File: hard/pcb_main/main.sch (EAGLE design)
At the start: 155 parts

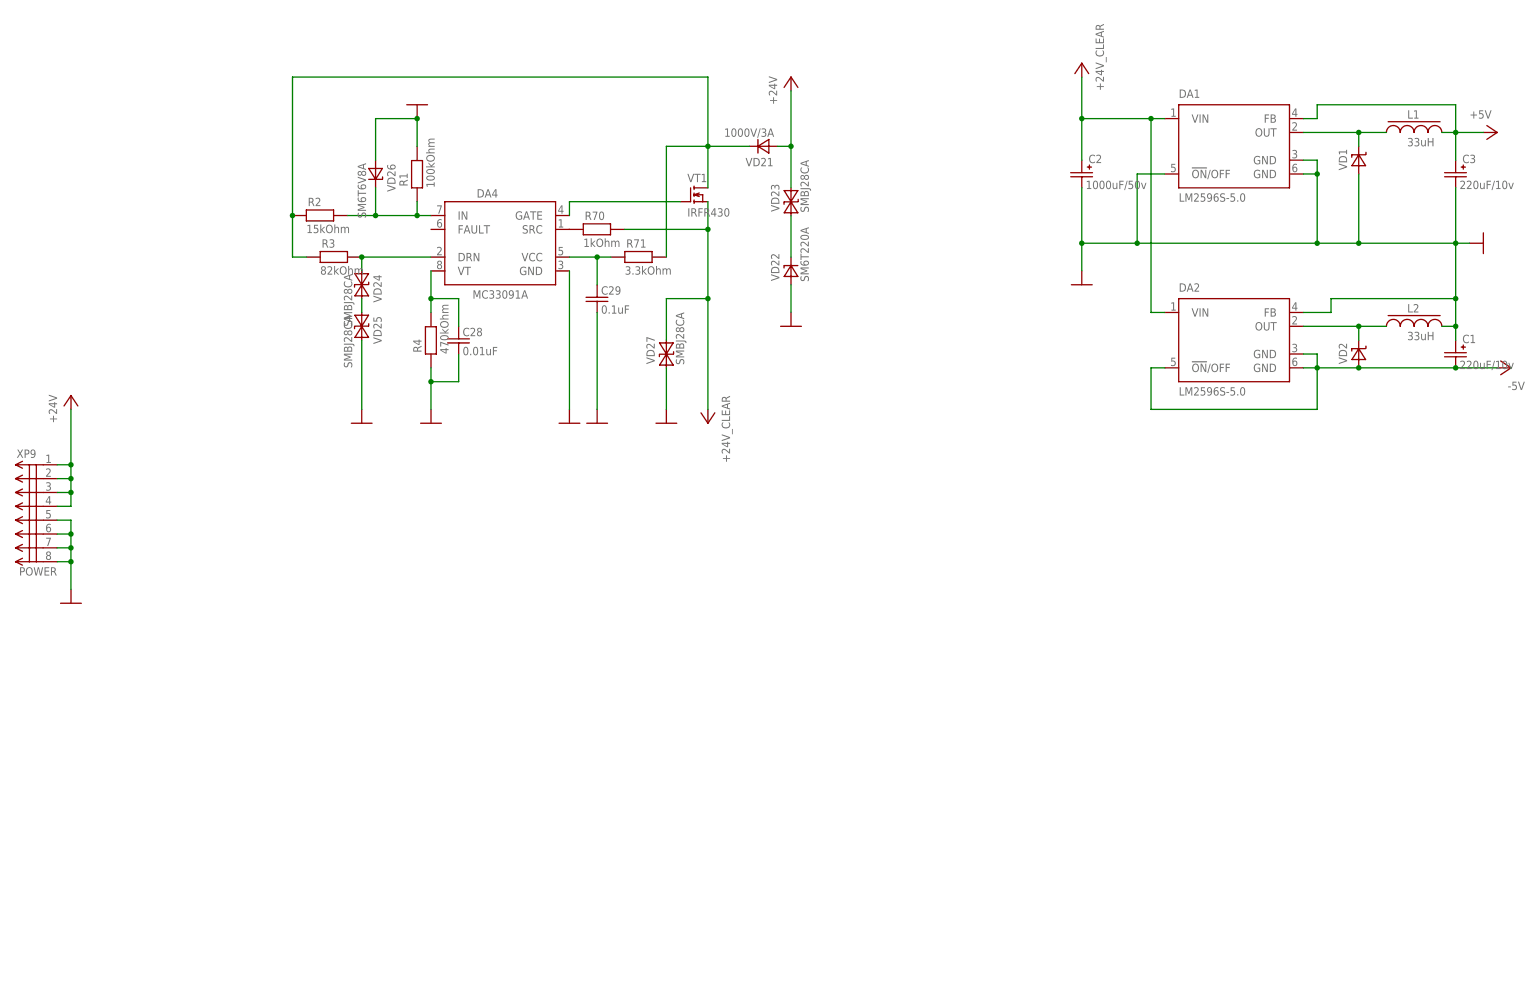
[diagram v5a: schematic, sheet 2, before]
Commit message: load dump protection routed
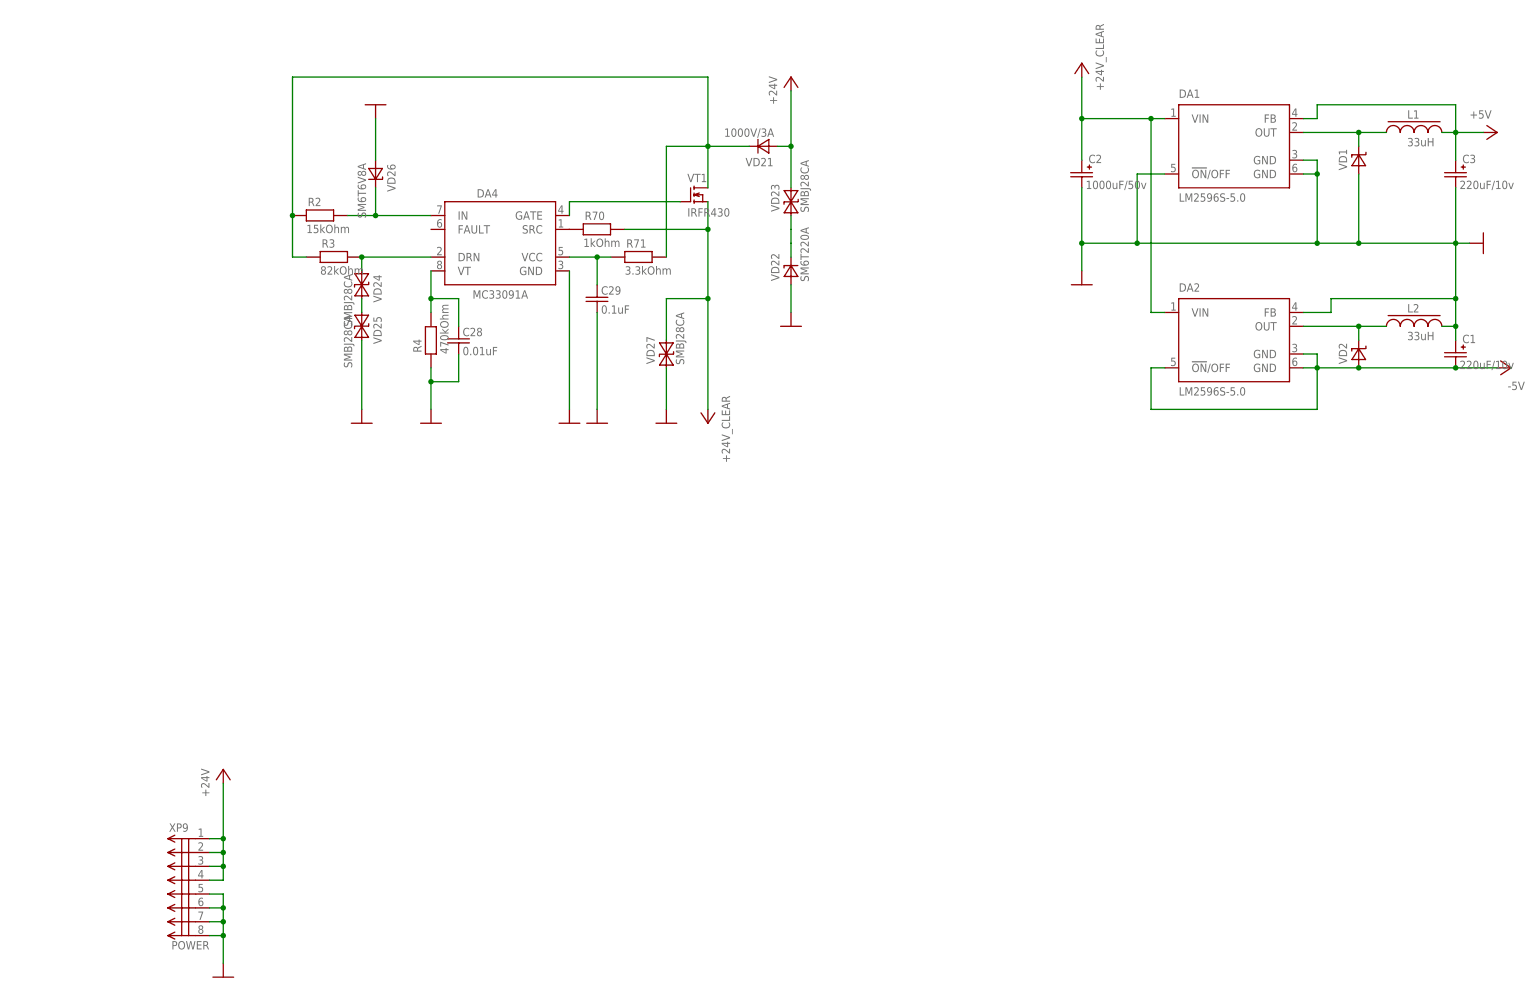
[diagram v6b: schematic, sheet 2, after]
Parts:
- removed R1: 100kOhm, rcl:R-EU_R0603
- JP1, JP2, JP3, JP4, JP5, JP6: value STAND-OFF -> STAND-OFFLONG; device SparkFun:STAND-OFF -> mount:STAND-OFFLONG
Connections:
- net GND: no longer R1.2
- net N$25: no longer R1.1
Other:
- moved on the sheet: XP9
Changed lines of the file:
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@@
 <setting verticaltext="up"/>
 </settings>
-<grid distance="0.1" unitdist="inch" unit="inch" style="lines" multiple="1" display="yes" altdistance="0.01" altunitdist="inch" altunit="inch"/>
+<grid distance="0.1" unitdist="inch" unit="inch" style="lines" multiple="1" display="no" altdistance="0.01" altunitdist="inch" altunit="inch"/>
 <layers>
 <layer number="1" name="Top" color="4" fill="1" visible="no" active="no"/>
@@
 <attribute name="PARTNO" value="*"/>
 </part>
-<part name="JP1" library="SparkFun" deviceset="STAND-OFF" device="">
+<part name="JP1" library="mount" deviceset="STAND-OFF" device="LONG">
 <attribute name="BOM" value="EXCLUDE"/>
 </part>
-<part name="JP2" library="SparkFun" deviceset="STAND-OFF" device="">
+<part name="JP2" library="mount" deviceset="STAND-OFF" device="LONG">
 <attribute name="BOM" value="EXCLUDE"/>
 </part>
-<part name="JP3" library="SparkFun" deviceset="STAND-OFF" device="">
+<part name="JP3" library="mount" deviceset="STAND-OFF" device="LONG">
 <attribute name="BOM" value="EXCLUDE"/>
 </part>
-<part name="JP4" library="SparkFun" deviceset="STAND-OFF" device="">
+<part name="JP4" library="mount" deviceset="STAND-OFF" device="LONG">
 <attribute name="BOM" value="EXCLUDE"/>
 </part>
-<part name="JP5" library="SparkFun" deviceset="STAND-OFF" device="">
+<part name="JP5" library="mount" deviceset="STAND-OFF" device="LONG">
 <attribute name="BOM" value="EXCLUDE"/>
 </part>
-<part name="JP6" library="SparkFun" deviceset="STAND-OFF" device="">
+<part name="JP6" library="mount" deviceset="STAND-OFF" device="LONG">
 <attribute name="BOM" value="EXCLUDE"/>
 </part>
@@
 <part name="GND29" library="supply" deviceset="GND" device=""/>
 <part name="P+3" library="supply" deviceset="+24V" device=""/>
-<part name="R1" library="rcl" deviceset="R-EU_" device="R0603" value="100kOhm">
-<attribute name="PARTNO" value="RC0603FR-13100KL"/>
-</part>
 <part name="C29" library="rcl" deviceset="C-EU" device="C0603" value="0.1uF">
 <attribute name="PARTNO" value="C0603C104K5RACTU"/>
@@
 <attribute name="PARTNO" value="LM2596S-5.0" x="208.28" y="139.7" size="1.778" layer="96" display="off"/>
 </instance>
-<instance part="XP9" gate="G$1" x="-7.62" y="116.84" rot="MR0">
-<attribute name="PARTNO" value="*" x="-7.62" y="116.84" size="1.524" layer="96" display="off"/>
-</instance>
-<instance part="GND26" gate="1" x="-5.08" y="93.98"/>
+<instance part="XP9" gate="G$1" x="20.32" y="48.26" rot="MR0">
+<attribute name="PARTNO" value="*" x="20.32" y="48.26" size="1.524" layer="96" display="off"/>
+</instance>
+<instance part="GND26" gate="1" x="22.86" y="25.4"/>
 <instance part="P+20" gate="G$1" x="180.34" y="187.96" rot="MR0"/>
-<instance part="P+19" gate="1" x="-5.08" y="129.54"/>
+<instance part="P+19" gate="1" x="22.86" y="60.96"/>
 <instance part="P+1" gate="1" x="256.54" y="177.8" rot="R270"/>
 <instance part="GND28" gate="1" x="251.46" y="157.48" rot="R90"/>
@@
 <instance part="GND29" gate="1" x="127" y="144.78"/>
 <instance part="P+3" gate="1" x="127" y="187.96"/>
-<instance part="R1" gate="G$1" x="58.42" y="170.18" rot="R90">
-<attribute name="PARTNO" value="RC0603FR-13100KL" x="58.42" y="170.18" size="1.778" layer="96" rot="R90" display="off"/>
-</instance>
 <instance part="C29" gate="G$1" x="91.44" y="147.32">
 <attribute name="PARTNO" value="C0603C104K5RACTU" x="91.44" y="147.32" size="1.524" layer="96" display="off"/>
@@
 <attribute name="PARTNO" x="99.06" y="154.94" size="1.778" layer="96" display="off"/>
 </instance>
-<instance part="GND33" gate="1" x="58.42" y="180.34" rot="R180"/>
+<instance part="GND33" gate="1" x="50.8" y="180.34" rot="R180"/>
 <instance part="VD26" gate="G$1" x="50.8" y="170.18" rot="R270">
 <attribute name="PARTNO" x="50.8" y="170.18" size="1.778" layer="96" rot="R90" display="off"/>
@@
 <segment>
 <pinref part="GND26" gate="1" pin="GND"/>
-<wire x1="-5.08" y1="93.98" x2="-5.08" y2="99.06" width="0.1524" layer="91"/>
+<wire x1="22.86" y1="25.4" x2="22.86" y2="30.48" width="0.1524" layer="91"/>
 <pinref part="XP9" gate="G$1" pin="8"/>
-<wire x1="-5.08" y1="99.06" x2="-7.62" y2="99.06" width="0.1524" layer="91"/>
-<wire x1="-5.08" y1="99.06" x2="-5.08" y2="101.6" width="0.1524" layer="91"/>
-<junction x="-5.08" y="99.06"/>
+<wire x1="22.86" y1="30.48" x2="20.32" y2="30.48" width="0.1524" layer="91"/>
+<wire x1="22.86" y1="30.48" x2="22.86" y2="33.02" width="0.1524" layer="91"/>
+<junction x="22.86" y="30.48"/>
 <pinref part="XP9" gate="G$1" pin="7"/>
-<wire x1="-5.08" y1="101.6" x2="-7.62" y2="101.6" width="0.1524" layer="91"/>
-<wire x1="-5.08" y1="101.6" x2="-5.08" y2="104.14" width="0.1524" layer="91"/>
-<junction x="-5.08" y="101.6"/>
+<wire x1="22.86" y1="33.02" x2="20.32" y2="33.02" width="0.1524" layer="91"/>
+<wire x1="22.86" y1="33.02" x2="22.86" y2="35.56" width="0.1524" layer="91"/>
+<junction x="22.86" y="33.02"/>
 <pinref part="XP9" gate="G$1" pin="6"/>
-<wire x1="-5.08" y1="104.14" x2="-7.62" y2="104.14" width="0.1524" layer="91"/>
-<wire x1="-5.08" y1="104.14" x2="-5.08" y2="106.68" width="0.1524" layer="91"/>
-<junction x="-5.08" y="104.14"/>
+<wire x1="22.86" y1="35.56" x2="20.32" y2="35.56" width="0.1524" layer="91"/>
+<wire x1="22.86" y1="35.56" x2="22.86" y2="38.1" width="0.1524" layer="91"/>
+<junction x="22.86" y="35.56"/>
 <pinref part="XP9" gate="G$1" pin="5"/>
-<wire x1="-5.08" y1="106.68" x2="-7.62" y2="106.68" width="0.1524" layer="91"/>
+<wire x1="22.86" y1="38.1" x2="20.32" y2="38.1" width="0.1524" layer="91"/>
 </segment>
 <segment>
@@
 </segment>
 <segment>
-<pinref part="R1" gate="G$1" pin="2"/>
 <pinref part="GND33" gate="1" pin="GND"/>
-<wire x1="58.42" y1="175.26" x2="58.42" y2="180.34" width="0.1524" layer="91"/>
 <wire x1="50.8" y1="172.72" x2="50.8" y2="180.34" width="0.1524" layer="91"/>
-<wire x1="50.8" y1="180.34" x2="58.42" y2="180.34" width="0.1524" layer="91"/>
-<junction x="58.42" y="180.34"/>
 <pinref part="VD26" gate="G$1" pin="A"/>
 </segment>
@@
 <segment>
 <pinref part="XP9" gate="G$1" pin="4"/>
-<wire x1="-7.62" y1="109.22" x2="-5.08" y2="109.22" width="0.1524" layer="91"/>
-<wire x1="-5.08" y1="109.22" x2="-5.08" y2="111.76" width="0.1524" layer="91"/>
+<wire x1="20.32" y1="40.64" x2="22.86" y2="40.64" width="0.1524" layer="91"/>
+<wire x1="22.86" y1="40.64" x2="22.86" y2="43.18" width="0.1524" layer="91"/>
 <pinref part="XP9" gate="G$1" pin="3"/>
-<wire x1="-5.08" y1="111.76" x2="-7.62" y2="111.76" width="0.1524" layer="91"/>
-<wire x1="-5.08" y1="111.76" x2="-5.08" y2="114.3" width="0.1524" layer="91"/>
-<junction x="-5.08" y="111.76"/>
+<wire x1="22.86" y1="43.18" x2="20.32" y2="43.18" width="0.1524" layer="91"/>
+<wire x1="22.86" y1="43.18" x2="22.86" y2="45.72" width="0.1524" layer="91"/>
+<junction x="22.86" y="43.18"/>
 <pinref part="XP9" gate="G$1" pin="2"/>
-<wire x1="-5.08" y1="114.3" x2="-7.62" y2="114.3" width="0.1524" layer="91"/>
+<wire x1="22.86" y1="45.72" x2="20.32" y2="45.72" width="0.1524" layer="91"/>
 <pinref part="XP9" gate="G$1" pin="1"/>
-<wire x1="-7.62" y1="116.84" x2="-5.08" y2="116.84" width="0.1524" layer="91"/>
-<wire x1="-5.08" y1="114.3" x2="-5.08" y2="116.84" width="0.1524" layer="91"/>
-<junction x="-5.08" y="114.3"/>
+<wire x1="20.32" y1="48.26" x2="22.86" y2="48.26" width="0.1524" layer="91"/>
+<wire x1="22.86" y1="45.72" x2="22.86" y2="48.26" width="0.1524" layer="91"/>
+<junction x="22.86" y="45.72"/>
 <pinref part="P+19" gate="1" pin="+24V"/>
-<wire x1="-5.08" y1="116.84" x2="-5.08" y2="127" width="0.1524" layer="91"/>
-<junction x="-5.08" y="116.84"/>
+<wire x1="22.86" y1="48.26" x2="22.86" y2="58.42" width="0.1524" layer="91"/>
+<junction x="22.86" y="48.26"/>
 </segment>
 <segment>
@@
 <pinref part="VD22" gate="G$1" pin="C"/>
 <pinref part="VD23" gate="G$1" pin="A2"/>
-<wire x1="127" y1="154.94" x2="127" y2="162.56" width="0.1524" layer="91"/>
+<wire x1="127" y1="154.94" x2="127" y2="157.48" width="0.1524" layer="91"/>
+<wire x1="127" y1="160.02" x2="127" y2="162.56" width="0.1524" layer="91"/>
+<wire x1="127" y1="160.02" x2="127" y2="157.48" width="0.1524" layer="91"/>
 </segment>
 </net>
@@
 <pinref part="R2" gate="G$1" pin="2"/>
 <wire x1="45.72" y1="162.56" x2="50.8" y2="162.56" width="0.1524" layer="91"/>
-<pinref part="R1" gate="G$1" pin="1"/>
-<wire x1="50.8" y1="162.56" x2="58.42" y2="162.56" width="0.1524" layer="91"/>
-<wire x1="58.42" y1="162.56" x2="60.96" y2="162.56" width="0.1524" layer="91"/>
-<wire x1="58.42" y1="165.1" x2="58.42" y2="162.56" width="0.1524" layer="91"/>
-<junction x="58.42" y="162.56"/>
+<wire x1="50.8" y1="162.56" x2="60.96" y2="162.56" width="0.1524" layer="91"/>
 <junction x="50.8" y="162.56"/>
 <pinref part="VD26" gate="G$1" pin="C"/>
